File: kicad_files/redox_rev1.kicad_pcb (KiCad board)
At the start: 2 copper layers, 162.2 x 126.5 mm, 88 parts, among them K0 KEYSW, K1 KEYSW, K10 KEYSW, K11 KEYSW, K12 KEYSW, K13 KEYSW, K14 KEYSW, K15 KEYSW, K16 KEYSW, K2 KEYSW, K20 KEYSW, K21 KEYSW, K22 KEYSW, K23 KEYSW, K24 KEYSW, K25 KEYSW, K26 KEYSW, K3 KEYSW, K30 KEYSW, K31 KEYSW, K32 KEYSW, K33 KEYSW, K34 KEYSW, K35 KEYSW, K36 KEYSW, K4 KEYSW, K40 KEYSW, K41 KEYSW, K42 KEYSW, K43 KEYSW, K44 KEYSW, K45 KEYSW, K46 KEYSW, K5 KEYSW, K6 KEYSW

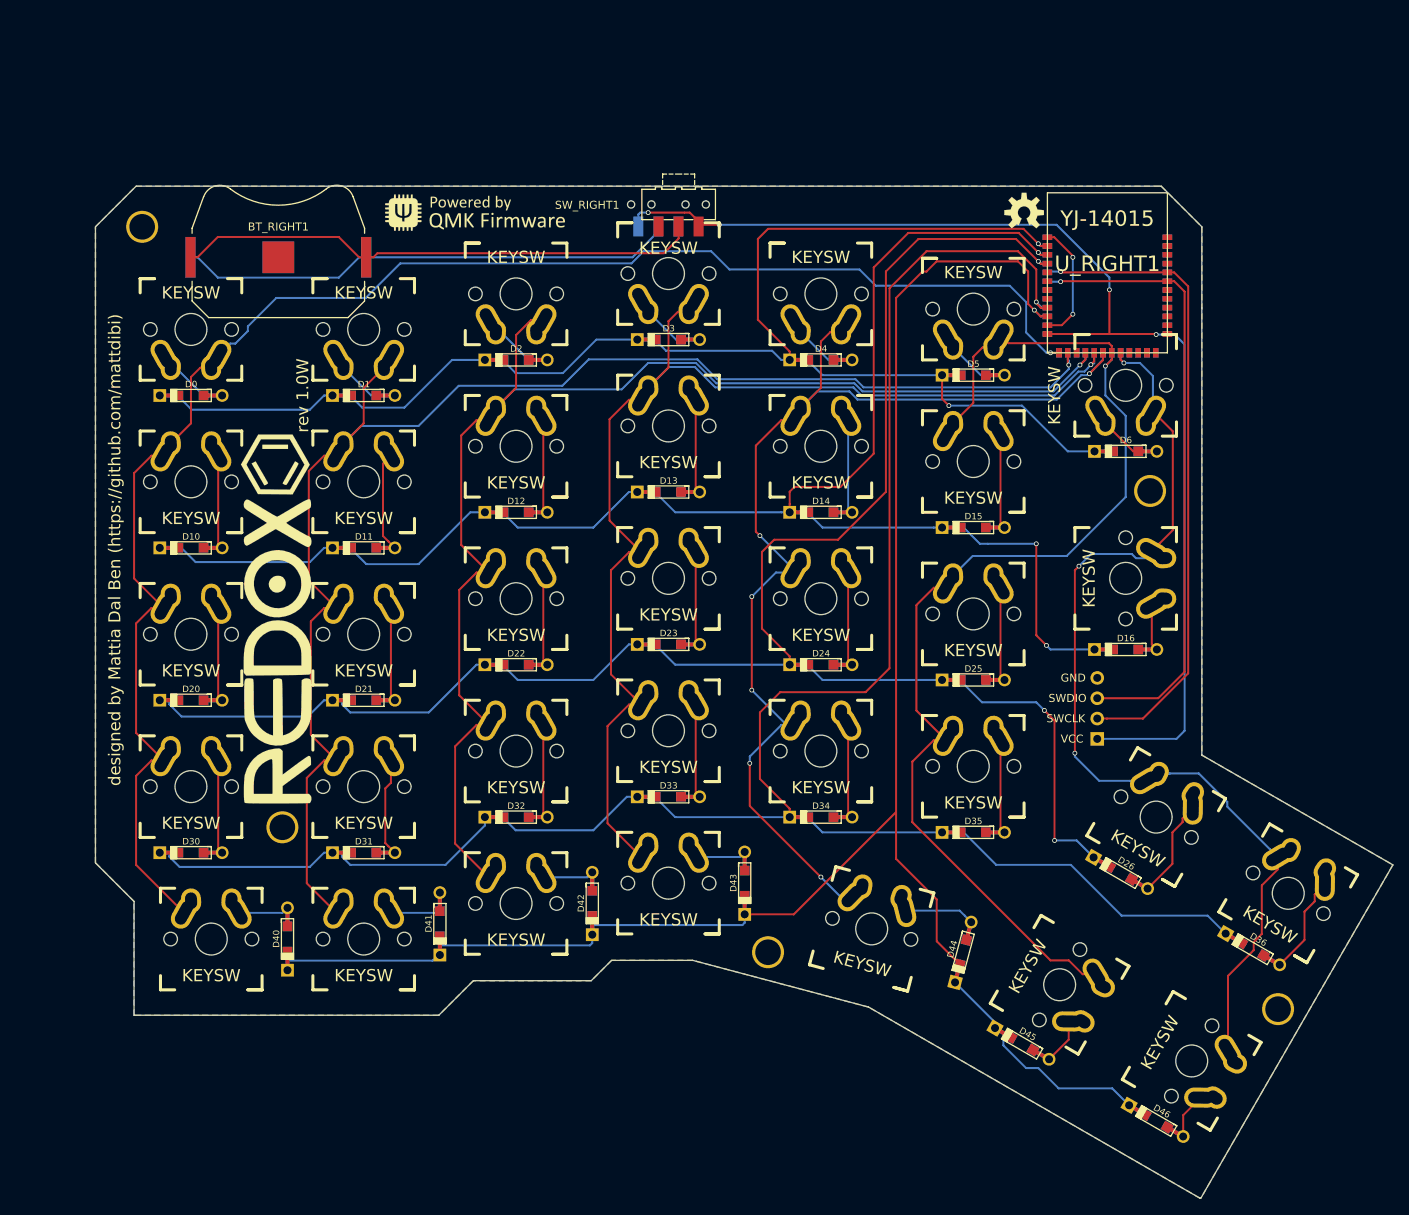
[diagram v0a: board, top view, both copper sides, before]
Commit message: First production
* NFSW GND not connected
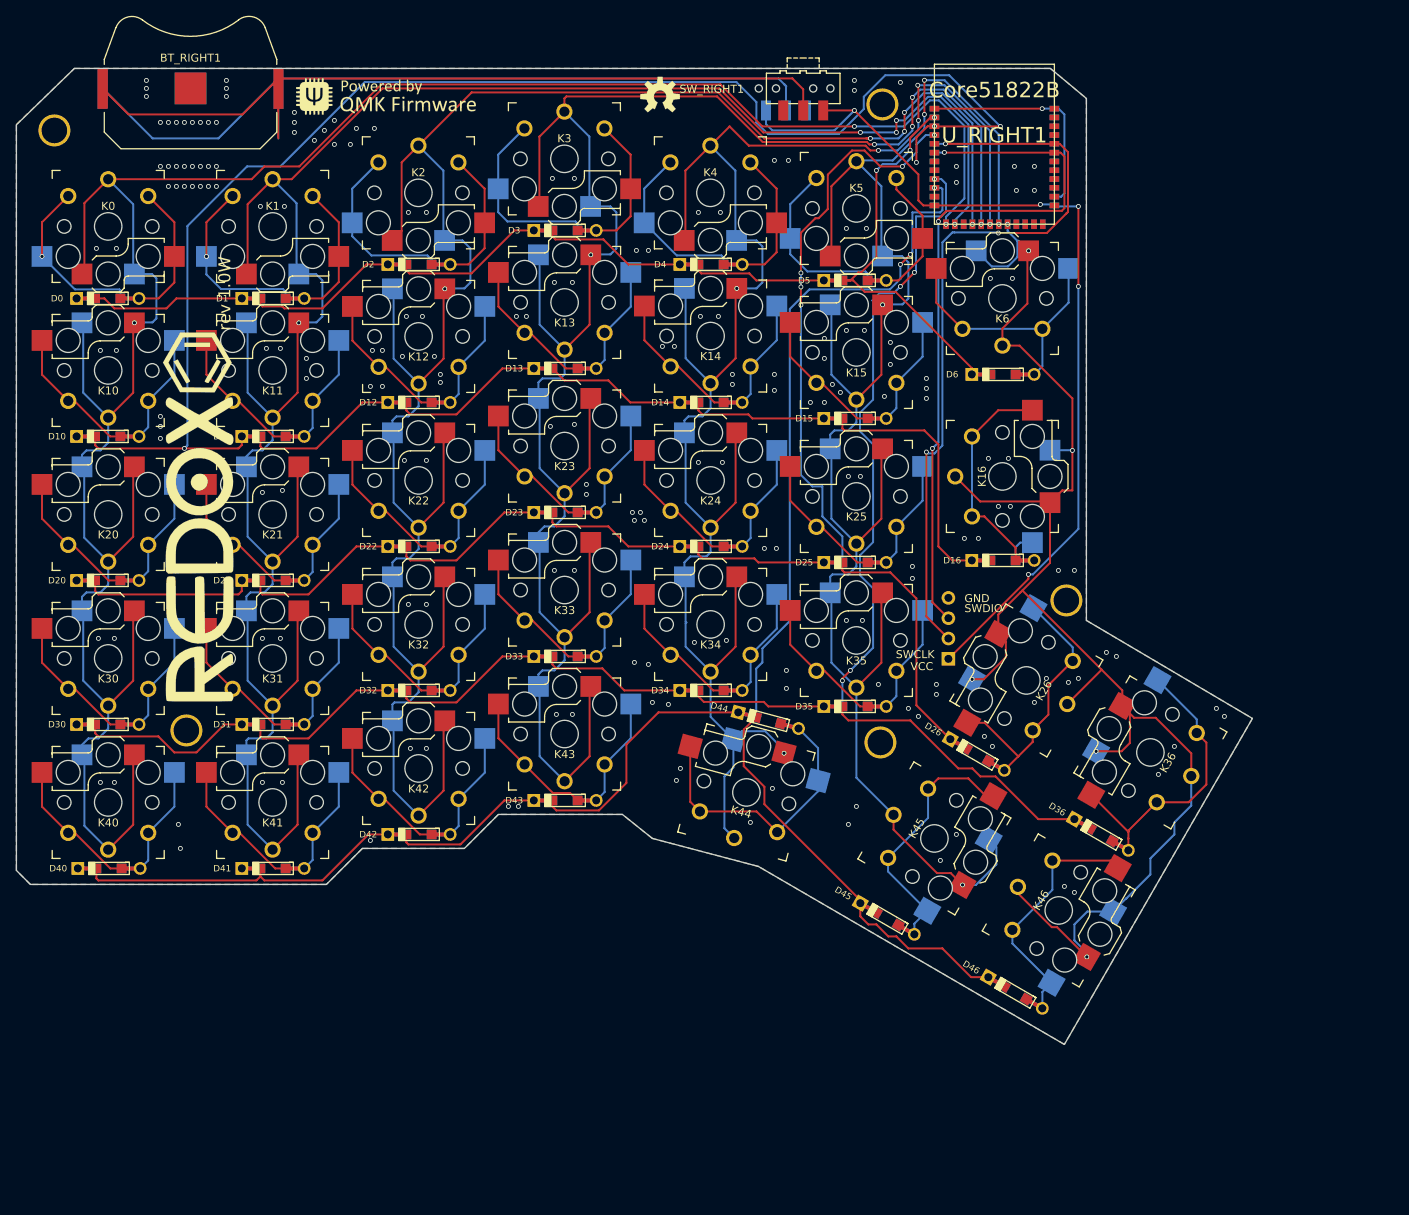
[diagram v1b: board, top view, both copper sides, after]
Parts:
- J_PROG_PORT1: footprint Connector_PinHeader_2.54mm:PinHeader_1x04_P2.54mm_Horizontal -> Connector_PinHeader_2.54mm:PinHeader_1x04_P2.54mm_Vertical
- K0, K10, K20, K30, K44: footprint myparts:Mx_Alps_125-dualside -> Keebio-Parts:Kailh_socket_PG1350_optional_reversible_125
- K1, K11, K12, K13, K14, K15, K2, K21, K22, K23, K24, K25, K26, K3, K31, K32, K33, K34, K35, K36, K4, K41, K42, K43, K5, K6: footprint canadian_footprints:Mx_Alps_100-dualside -> Keebio-Parts:Kailh_socket_PG1350_optional_reversible_100
- K16, K45, K46: footprint canadian_footprints:Mx_Alps_150-dualsided -> Keebio-Parts:Kailh_socket_PG1350_optional_reversible_150
- K40: footprint canadian_footprints:Mx_Alps_100-dualside -> Keebio-Parts:Kailh_socket_PG1350_optional_reversible_125
- U_LEFT1, U_RIGHT1: value YJ-14015 -> Core51822B; footprint YJ-14015:MY-YJ-14015-Module -> Keebio-Parts:MY-YJ-14015-Module
- moved HOLE_M3 59.9 mm to (177.6, 118.3)
- moved HOLE_M3 58.8 mm to (177.9, 38.5)
- moved HOLE_M3 57.7 mm to (200.9, 100.5)
- moved ? 47.8 mm to (150.1, 37.6)
- moved ? 47.7 mm to (150.1, 37.5)
- moved D44 37.8 mm to (163.6, 115.5), turned to 165 degrees
- moved K46 25.1 mm to (199.9, 139.3)
- moved D43 24.7 mm to (138.2, 125.5), turned to 180 degrees
- moved K36 24.6 mm to (211.4, 119.5), turned to 60 degrees
- moved K45 24.1 mm to (184.4, 130.3)
- moved D40 24.0 mm to (81.2, 134.1), turned to 180 degrees
- moved D46 23.8 mm to (194.5, 149.6)
- moved BT_LEFT1 23.8 mm to (91.4, 36.5)
- moved BT_RIGHT1 23.8 mm to (91.4, 36.5)
- moved D36 23.7 mm to (205.2, 129.8)
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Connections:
- SW_LEFT1 pad 3: Net-(SW_LEFT1-Pad3) -> unconnected-(SW_LEFT1-C-Pad3)
- SW_RIGHT1 pad 3: Net-(SW_RIGHT1-Pad3) -> unconnected-(SW_RIGHT1-C-Pad3)
- U_LEFT1 pad 10: Net-(U_LEFT1-Pad10) -> unconnected-(U_LEFT1-P29-Pad10)
- U_LEFT1 pad 13: Net-(U_LEFT1-Pad13) -> unconnected-(U_LEFT1-P30-Pad13)
- U_LEFT1 pad 14: Net-(U_LEFT1-Pad14) -> unconnected-(U_LEFT1-P00-Pad14)
- U_LEFT1 pad 15: Net-(U_LEFT1-Pad15) -> unconnected-(U_LEFT1-P01-Pad15)
- U_LEFT1 pad 16: Net-(U_LEFT1-Pad16) -> unconnected-(U_LEFT1-P02-Pad16)
- U_LEFT1 pad 2: Net-(U_LEFT1-Pad2) -> unconnected-(U_LEFT1-P21-Pad2)
- U_LEFT1 pad 22: Net-(U_LEFT1-Pad22) -> unconnected-(U_LEFT1-P08-Pad22)
- U_LEFT1 pad 25: Net-(U_LEFT1-Pad25) -> unconnected-(U_LEFT1-P11-Pad25)
- U_LEFT1 pad 26: Net-(U_LEFT1-Pad26) -> unconnected-(U_LEFT1-P12-Pad26)
- U_LEFT1 pad 29: Net-(U_LEFT1-Pad29) -> unconnected-(U_LEFT1-P15-Pad29)
- U_LEFT1 pad 3: Net-(U_LEFT1-Pad3) -> unconnected-(U_LEFT1-P22-Pad3)
- U_LEFT1 pad 30: Net-(U_LEFT1-Pad30) -> unconnected-(U_LEFT1-P16-Pad30)
- U_LEFT1 pad 36: Net-(U_LEFT1-Pad36) -> unconnected-(U_LEFT1-P20-Pad36)
- U_LEFT1 pad 4: Net-(U_LEFT1-Pad4) -> unconnected-(U_LEFT1-P23-Pad4)
- U_LEFT1 pad 5: Net-(U_LEFT1-Pad5) -> unconnected-(U_LEFT1-P24-Pad5)
- U_LEFT1 pad 6: Net-(U_LEFT1-Pad6) -> unconnected-(U_LEFT1-P25-Pad6)
- U_LEFT1 pad 7: Net-(U_LEFT1-Pad7) -> unconnected-(U_LEFT1-NC-Pad7)
- U_LEFT1 pad 8: Net-(U_LEFT1-Pad8) -> unconnected-(U_LEFT1-NC-Pad8)
- U_LEFT1 pad 9: Net-(U_LEFT1-Pad9) -> unconnected-(U_LEFT1-P28-Pad9)
- U_RIGHT1 pad 15: Net-(U_RIGHT1-Pad15) -> unconnected-(U_RIGHT1-P01-Pad15)
- U_RIGHT1 pad 21: Net-(U_RIGHT1-Pad21) -> unconnected-(U_RIGHT1-P07-Pad21)
- U_RIGHT1 pad 22: Net-(U_RIGHT1-Pad22) -> unconnected-(U_RIGHT1-P08-Pad22)
- U_RIGHT1 pad 23: Net-(U_RIGHT1-Pad23) -> unconnected-(U_RIGHT1-P09-Pad23)
- U_RIGHT1 pad 24: Net-(U_RIGHT1-Pad24) -> unconnected-(U_RIGHT1-P10-Pad24)
- U_RIGHT1 pad 25: Net-(U_RIGHT1-Pad25) -> unconnected-(U_RIGHT1-P11-Pad25)
- U_RIGHT1 pad 26: Net-(U_RIGHT1-Pad26) -> unconnected-(U_RIGHT1-P12-Pad26)
- U_RIGHT1 pad 27: Net-(U_RIGHT1-Pad27) -> unconnected-(U_RIGHT1-P13-Pad27)
- U_RIGHT1 pad 28: Net-(U_RIGHT1-Pad28) -> unconnected-(U_RIGHT1-P14-Pad28)
- U_RIGHT1 pad 29: Net-(U_RIGHT1-Pad29) -> unconnected-(U_RIGHT1-P15-Pad29)
- U_RIGHT1 pad 30: Net-(U_RIGHT1-Pad30) -> unconnected-(U_RIGHT1-P16-Pad30)
- U_RIGHT1 pad 33: Net-(U_RIGHT1-Pad33) -> unconnected-(U_RIGHT1-P17-Pad33)
- U_RIGHT1 pad 34: Net-(U_RIGHT1-Pad34) -> unconnected-(U_RIGHT1-P18-Pad34)
- U_RIGHT1 pad 35: Net-(U_RIGHT1-Pad35) -> unconnected-(U_RIGHT1-P19-Pad35)
- U_RIGHT1 pad 36: Net-(U_RIGHT1-Pad36) -> unconnected-(U_RIGHT1-P20-Pad36)
- U_RIGHT1 pad 5: Net-(U_RIGHT1-Pad5) -> unconnected-(U_RIGHT1-P24-Pad5)
- U_RIGHT1 pad 6: Net-(U_RIGHT1-Pad6) -> unconnected-(U_RIGHT1-P25-Pad6)
- U_RIGHT1 pad 7: Net-(U_RIGHT1-Pad7) -> unconnected-(U_RIGHT1-NC-Pad7)
- U_RIGHT1 pad 8: Net-(U_RIGHT1-Pad8) -> unconnected-(U_RIGHT1-NC-Pad8)
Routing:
- net col3: track 145.0 -> 244.7 mm, vias 1 -> 5
- net col1: track 181.0 -> 280.0 mm, vias 1 -> 5
- net col2: track 165.4 -> 261.8 mm, vias 1 -> 5
- net col0: track 202.8 -> 298.3 mm, vias 1 -> 3
- net row1: track 196.3 -> 288.5 mm, vias 3 -> 4
- net col4: track 137.5 -> 223.6 mm
- net col5: track 141.4 -> 214.0 mm, vias 1 -> 5
- net col6: track 123.2 -> 189.7 mm, vias 3 -> 6
- net row3: track 250.7 -> 210.1 mm, vias 1 -> 5
- net Net-(BT_LEFT1-+): track 62.5 -> 102.4 mm
- net row0: track 181.0 -> 141.4 mm, vias 2 -> 3
- net Net-(BT_RIGHT1-+): track 65.6 -> 101.5 mm
- net Net-(D3-A): track 5.53 -> 40.6 mm
- net Net-(D1-A): track 5.53 -> 40.1 mm, vias 0 -> 1
- net Net-(D5-A): track 5.53 -> 39.8 mm
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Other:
- board size 162.2 x 126.5 mm -> 154.5 x 122 mm
- net class Default removed
- board text removed: "designed by Mattia Dal Ben (https://github.com/mattdibi)"
